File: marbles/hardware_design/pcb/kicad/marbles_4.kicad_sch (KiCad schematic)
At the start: 61 parts

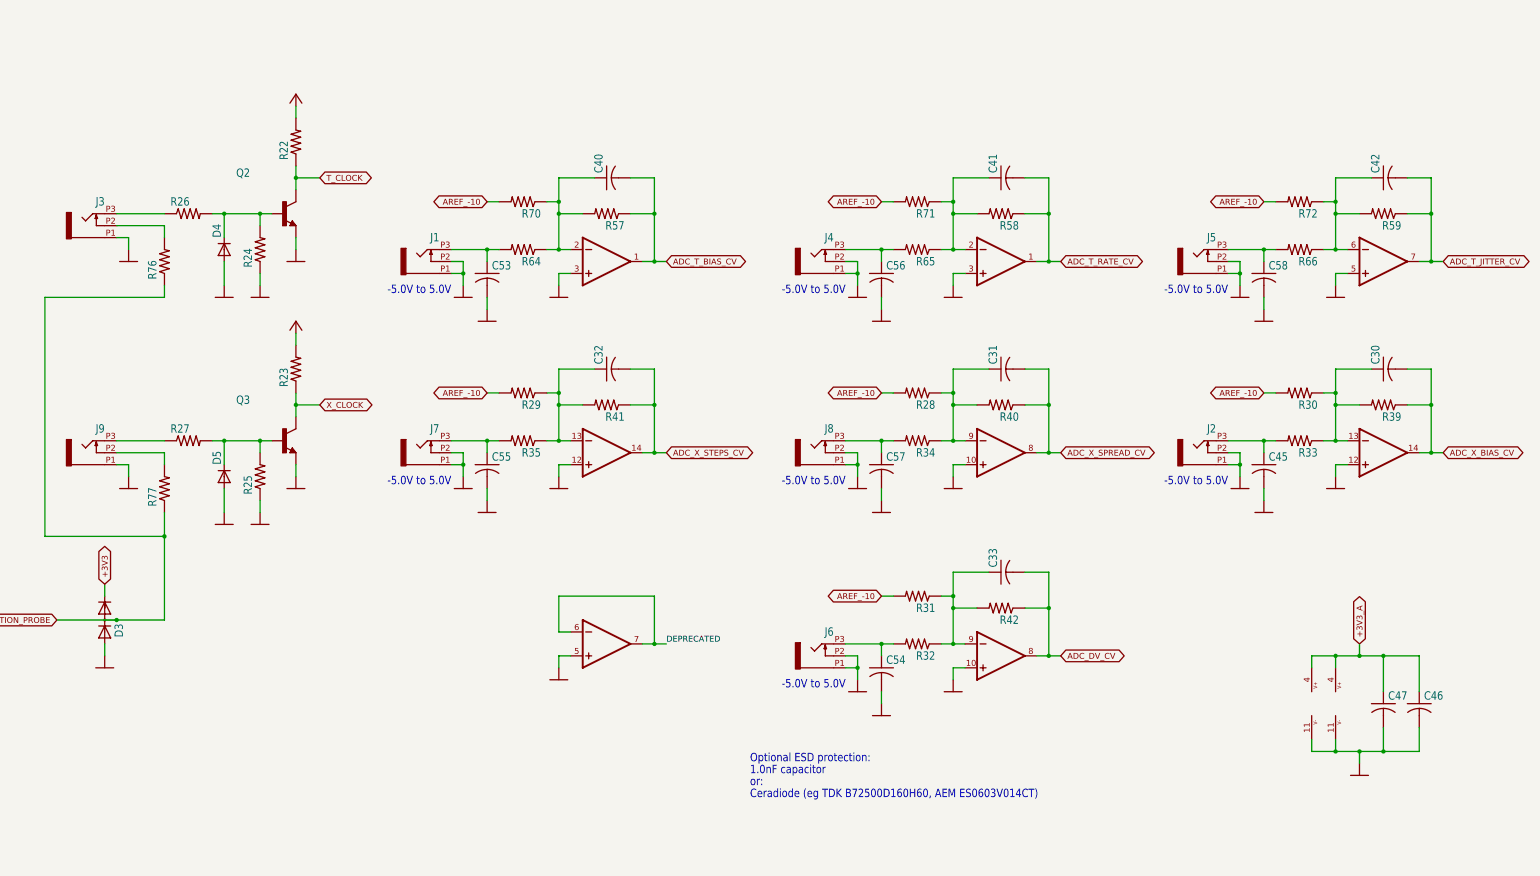
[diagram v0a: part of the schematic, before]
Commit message: added SMD LEDs in parallel with THT footprint
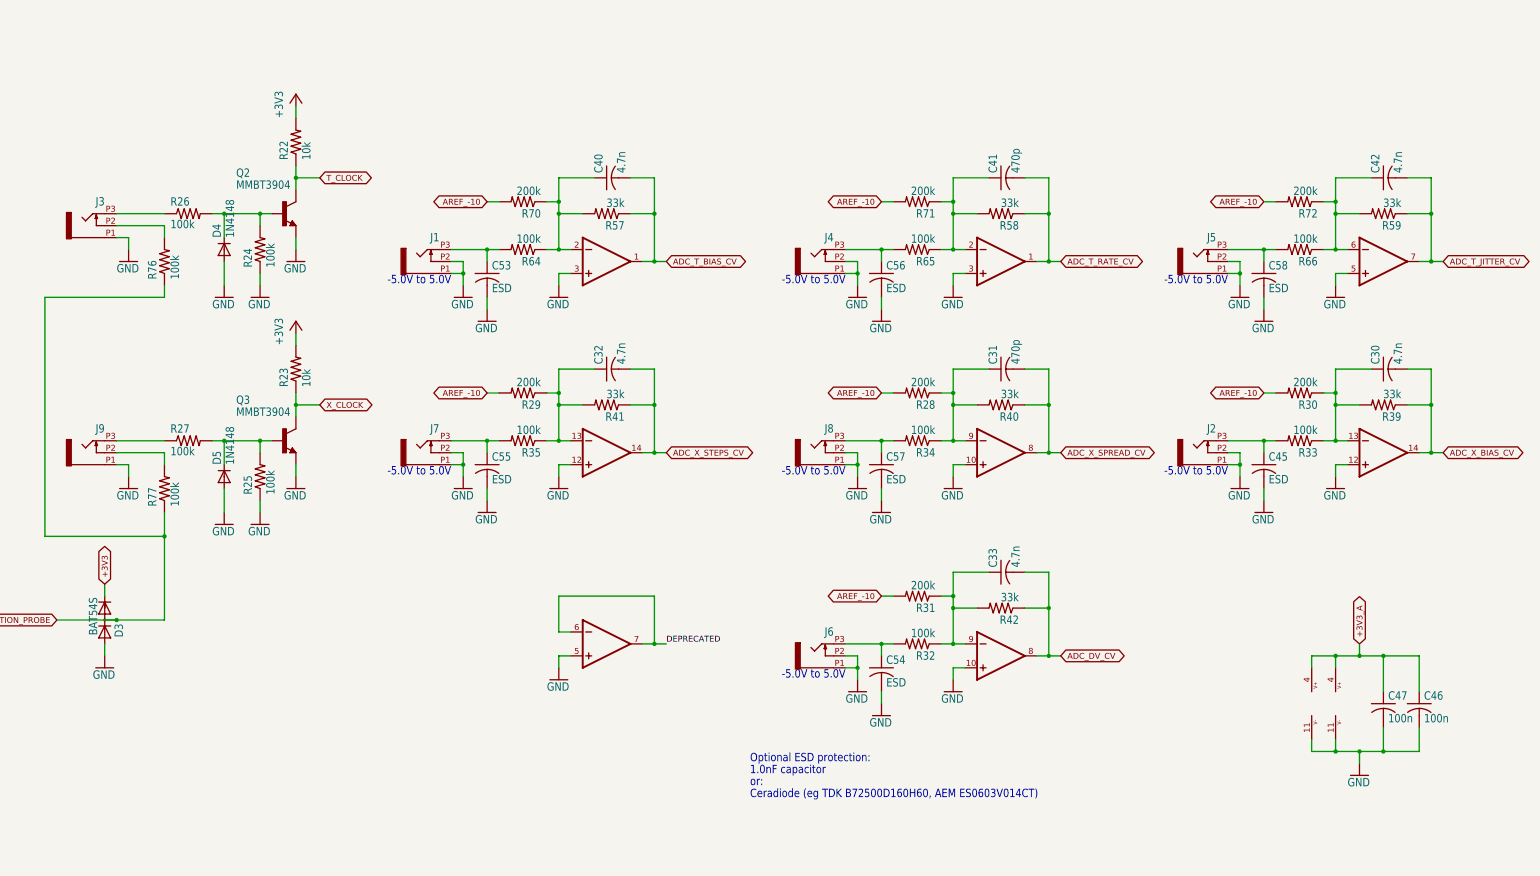
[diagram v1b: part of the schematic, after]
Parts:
- C30, C32, C33, C40, C42: value (none) -> 4.7n; footprint (none) -> marbles:C0402
- C31, C41: value (none) -> 470p; footprint (none) -> marbles:C0402
- C45, C53, C54, C55, C56, C57, C58: value (none) -> ESD; footprint (none) -> marbles:C0603
- C46, C47: value (none) -> 100n; footprint (none) -> marbles:C0402
- D3: value (none) -> BAT54S; footprint (none) -> marbles:SOT23
- D4, D5: value (none) -> 1N4148; footprint (none) -> marbles:SOD523
- IC5, IC6: value (none) -> MCP6004; footprint (none) -> marbles:TSSOP14_065
- J1, J2, J3, J4, J5, J6, J7, J8, J9: value (none) -> PJ301_THONKICONN6; footprint (none) -> marbles:WQP_PJ_301M6
- Q2, Q3: value (none) -> MMBT3904; footprint (none) -> marbles:SOT23-BEC
- R22, R23: value (none) -> 10k; footprint (none) -> marbles:R0402
- R24, R25, R26, R27, R32, R33, R34, R35, R64, R65, R66, R76, R77: value (none) -> 100k; footprint (none) -> marbles:R0402
- R28, R29, R30, R31, R70, R71, R72: value (none) -> 200k; footprint (none) -> marbles:R0402
- R39, R40, R41, R42, R57, R58, R59: value (none) -> 33k; footprint (none) -> marbles:R0402
